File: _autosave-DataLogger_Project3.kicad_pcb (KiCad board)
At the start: 2 copper layers, 50.3 x 30.9 mm, 29 parts, among them J1 Conn_01x04_Pin, J2 Conn_01x04_Pin, J3 Conn_01x09_Pin, J4 Conn_02x03_Odd_Even, U1 24LC1025, U2 24LC1025, U3 DS1337S_, U4 ATMEGA328P-AU, Y1 32.768kHz, Y2 16Mhz

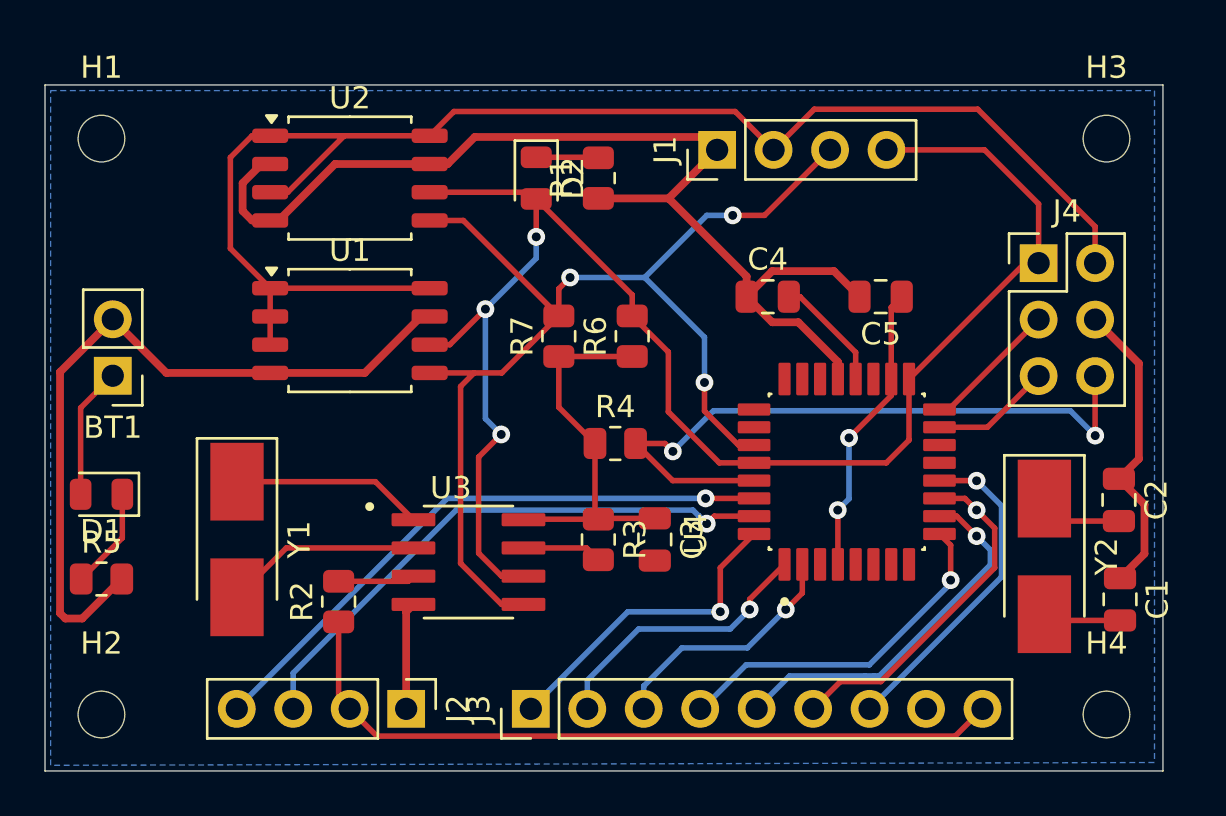
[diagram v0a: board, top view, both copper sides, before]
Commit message: finished routing 2 layer pcb
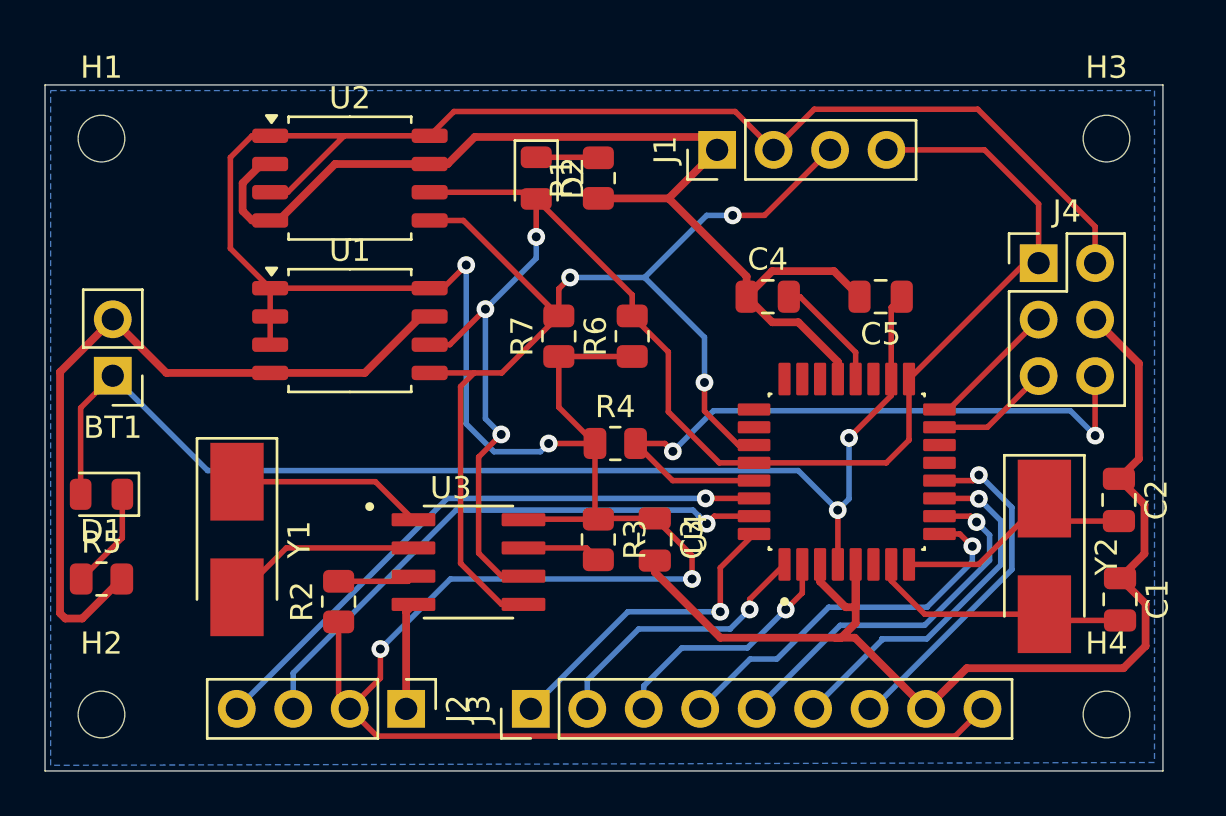
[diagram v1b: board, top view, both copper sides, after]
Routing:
- net GND: track 103.1 -> 141.7 mm
- net /VCC: track 116.7 -> 155.0 mm, vias 0 -> 4
- net Net-(BT1-+): track 19.2 -> 54.3 mm
- net Net-(U4-PB6): track 3.52 -> 11.8 mm
- net Net-(U4-PB7): track 3.77 -> 11.1 mm
- net /D5: track 16.0 -> 17.5 mm
- net /D8: track 14.9 -> 15.8 mm
- net /D7: track 15.6 -> 16.3 mm
- added copper zone on B.Cu, net GND
- removed copper zone on B.Cu, net /TX
